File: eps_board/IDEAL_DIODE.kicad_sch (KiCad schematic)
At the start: 3 parts, among them U19 LTC4415

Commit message: final version with 48 pin connector: all boost/buck converters, 2 switched batt lines (though not connected to bus yet
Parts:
- renumbered R96 to R103, R97 to R104, U19 to U23
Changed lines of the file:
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@@
 		(on_board yes)
 		(dnp no)
-		(property "Reference" "U19"
+		(property "Reference" "U23"
 			(at 144.78 67.945 0)
 			(effects
@@
 			(project ""
 				(path "/05170af6-30ef-4c3a-b972-f098085da1bc/00000000-0000-0000-0000-00005f71f783"
-					(reference "U19")
+					(reference "U23")
 					(unit 1)
 				)
@@
 		(on_board yes)
 		(dnp no)
-		(property "Reference" "R96"
+		(property "Reference" "R103"
 			(at 115.57 85.09 90)
 			(effects
@@
 			(project ""
 				(path "/05170af6-30ef-4c3a-b972-f098085da1bc/00000000-0000-0000-0000-00005f71f783"
-					(reference "R96")
+					(reference "R103")
 					(unit 1)
 				)
@@
 		(on_board yes)
 		(dnp no)
-		(property "Reference" "R97"
+		(property "Reference" "R104"
 			(at 115.57 92.71 90)
 			(effects
@@
 			(project ""
 				(path "/05170af6-30ef-4c3a-b972-f098085da1bc/00000000-0000-0000-0000-00005f71f783"
-					(reference "R97")
+					(reference "R104")
 					(unit 1)
 				)

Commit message: changed from 48 pin connector to 40 pic PCA connector. remove uarts, ensure reset pins for all system components, attention pin to iniate IRQ on all components
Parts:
- renumbered R103 to R98, R104 to R99, U23 to U16
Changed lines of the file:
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@@
 		(on_board yes)
 		(dnp no)
-		(property "Reference" "U23"
+		(property "Reference" "U16"
 			(at 144.78 67.945 0)
 			(effects
@@
 			(project ""
 				(path "/05170af6-30ef-4c3a-b972-f098085da1bc/00000000-0000-0000-0000-00005f71f783"
-					(reference "U23")
+					(reference "U16")
 					(unit 1)
 				)
@@
 		(on_board yes)
 		(dnp no)
-		(property "Reference" "R103"
+		(property "Reference" "R98"
 			(at 115.57 85.09 90)
 			(effects
@@
 			(project ""
 				(path "/05170af6-30ef-4c3a-b972-f098085da1bc/00000000-0000-0000-0000-00005f71f783"
-					(reference "R103")
+					(reference "R98")
 					(unit 1)
 				)
@@
 		(on_board yes)
 		(dnp no)
-		(property "Reference" "R104"
+		(property "Reference" "R99"
 			(at 115.57 92.71 90)
 			(effects
@@
 			(project ""
 				(path "/05170af6-30ef-4c3a-b972-f098085da1bc/00000000-0000-0000-0000-00005f71f783"
-					(reference "R104")
+					(reference "R99")
 					(unit 1)
 				)

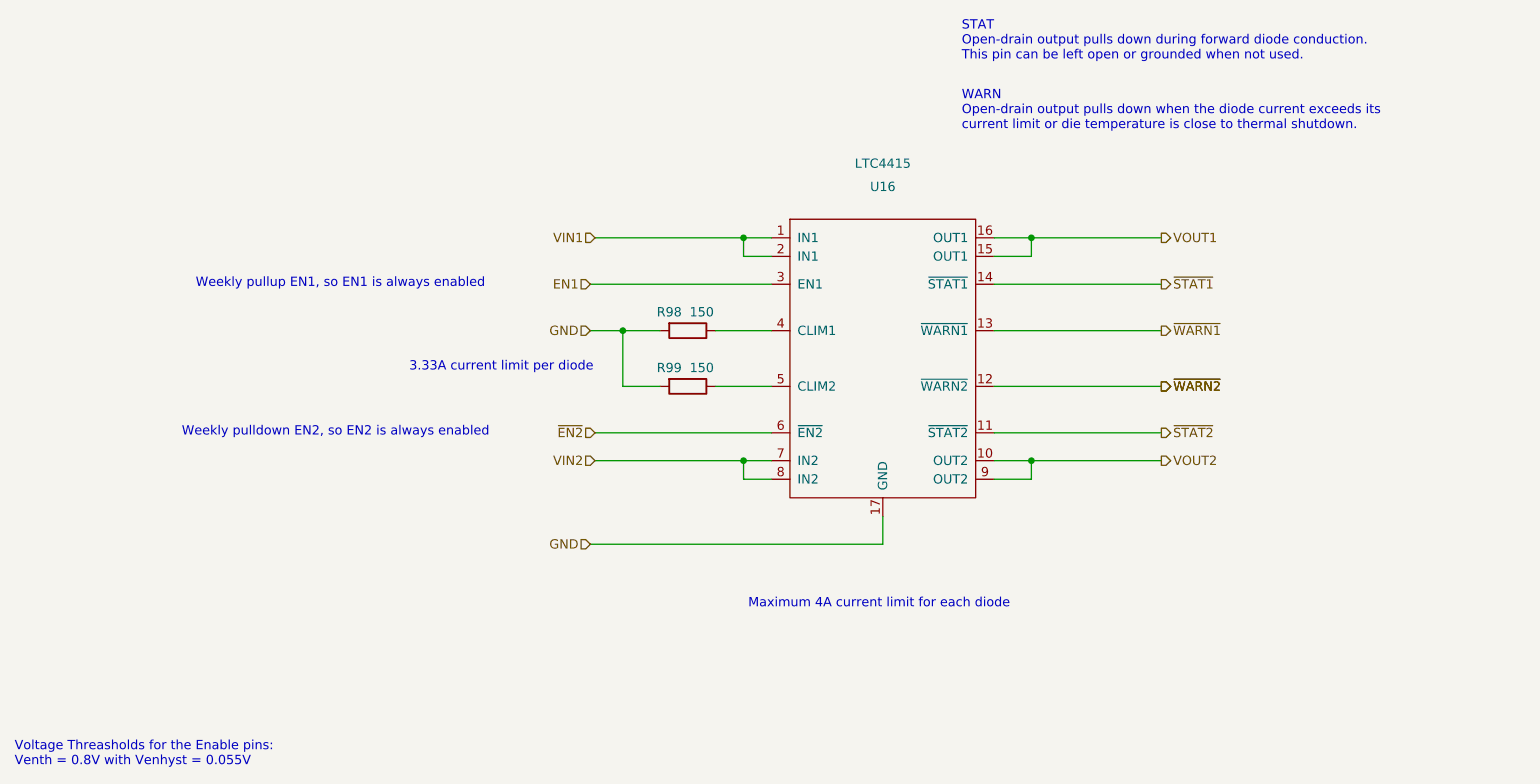
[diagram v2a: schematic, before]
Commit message: simply eps and automate startup conditions
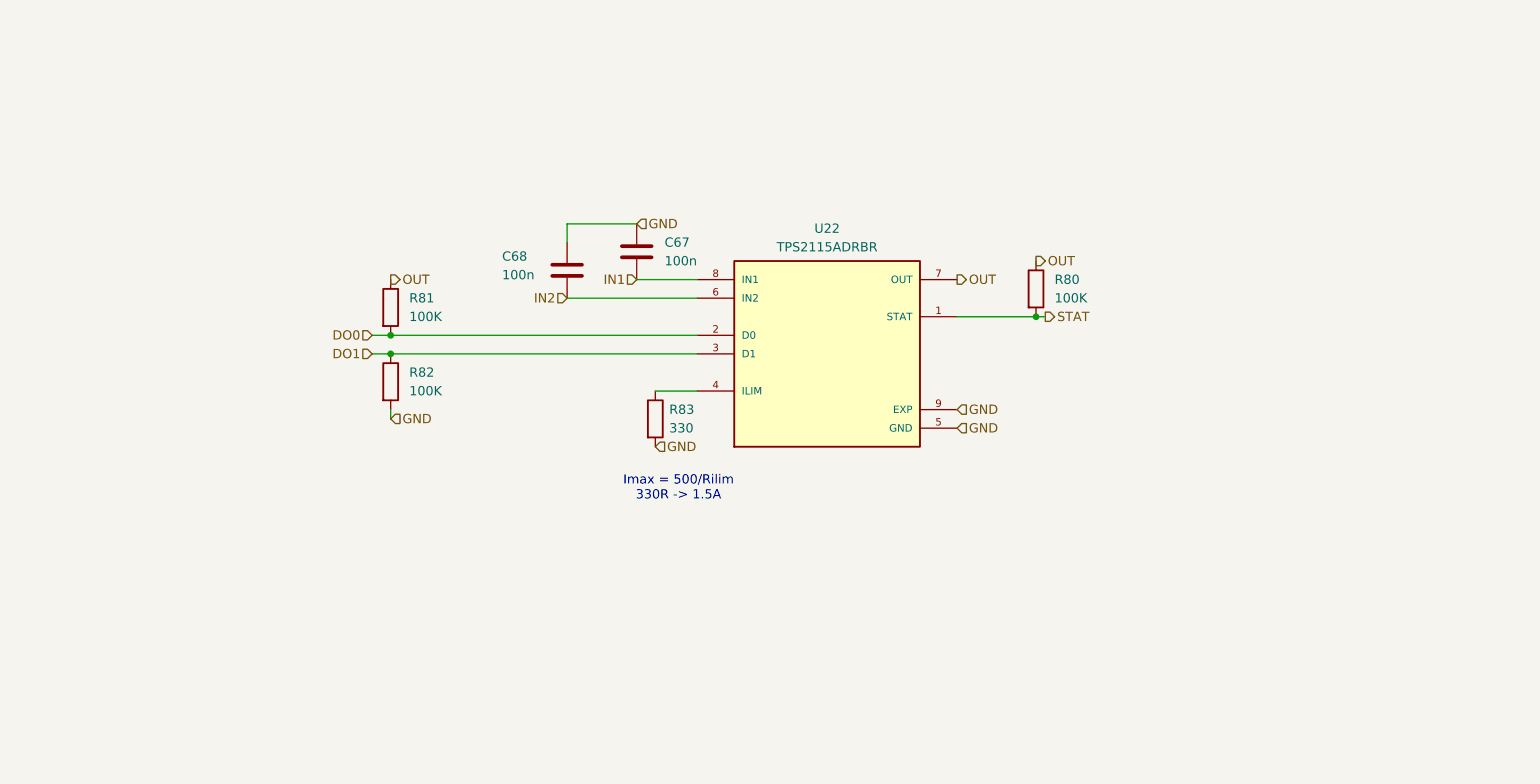
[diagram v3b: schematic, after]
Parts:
- removed R98, R99: 150, Resistor_SMD:R_0402_1005Metric_Pad0.72x0.64mm_HandSolder, symbol Device:R
- removed U16: LTC4415, Package_SO:MSOP-16-1EP_3x4.039mm_P0.5mm_EP1.651x2.845mm, symbol Project:LTC4415
- added C67, C68: 100n, Capacitor_SMD:C_0402_1005Metric_Pad0.74x0.62mm_HandSolder, symbol Device:C
- added R80, R81, R82: 100K, Resistor_SMD:R_0402_1005Metric_Pad0.72x0.64mm_HandSolder, symbol Device:R
- added R83: 330, Resistor_SMD:R_0402_1005Metric_Pad0.72x0.64mm_HandSolder, symbol Device:R
- added U22: TPS2115ADRBR, Common:SON65P300X300X100-9N, symbol Common:TPS2115ADRBR
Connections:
- net GND: now also C67.1, C68.1, R82.2, R83.2, U22.5 (GND), U22.9 (EXP)
- new net: R83.1, U22.4 (ILIM)
- new net DO0: R81.2, U22.2 (D0)
- new net DO1: R82.1, U22.3 (D1)
- new net IN1: C67.2, U22.8 (IN1)
- new net IN2: C68.2, U22.6 (IN2)
- new net OUT: R80.1, R81.1, U22.7 (OUT)
- new net STAT: R80.2, U22.1 (STAT)
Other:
- note added: "Imax = 500/Rilim 330R -> 1.5A"
- note removed: "3.33A current limit per diode"
- note removed: "Maximum 4A current limit for each diode"
- note removed: "STAT Open-drain output pulls down during forward diode conduction. This pin can be left open or grounded when not used."
- note removed: "Voltage Threasholds for the Enable pins: Venth = 0.8V with Venhyst = 0.055V"
- note removed: "WARN Open-drain output pulls down when the diode current exceeds its current limit or die temperature is close to thermal shutdown."
- note removed: "Weekly pulldown EN2, so EN2 is always enabled"
- note removed: "Weekly pullup EN1, so EN1 is always enabled"

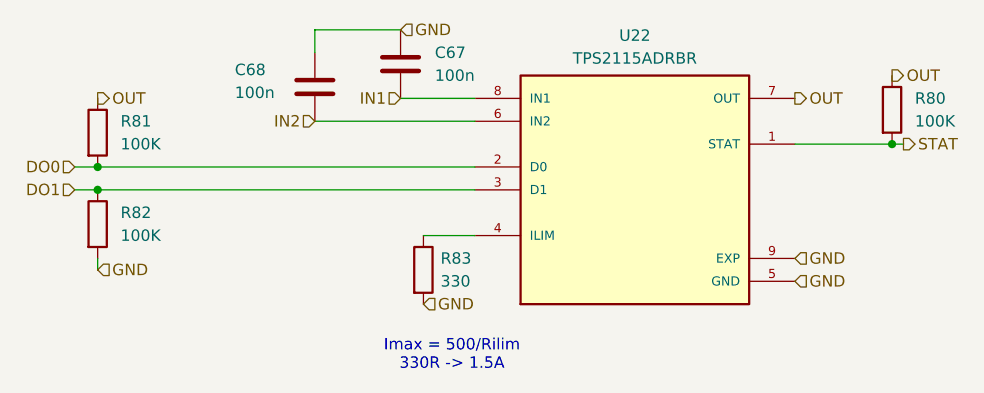
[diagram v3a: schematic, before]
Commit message: pcb and silk screen cleanup, interim
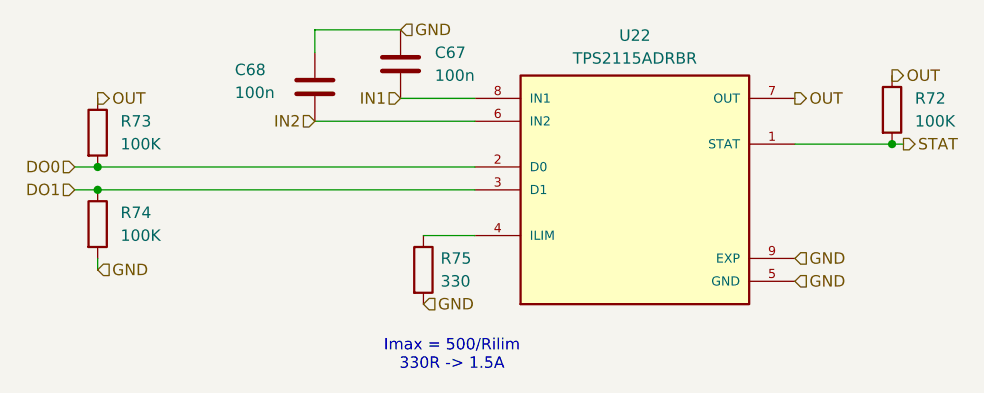
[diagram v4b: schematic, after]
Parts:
- renumbered R80 to R72, R81 to R73, R82 to R74, R83 to R75
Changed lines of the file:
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@@
 		(dnp no)
 		(fields_autoplaced yes)
-		(property "Reference" "R83"
+		(property "Reference" "R75"
 			(at 115.57 98.4249 0)
 			(effects
@@
 			(project "EPS"
 				(path "/05170af6-30ef-4c3a-b972-f098085da1bc/00000000-0000-0000-0000-00005f71f783"
-					(reference "R83")
+					(reference "R75")
 					(unit 1)
 				)
@@
 		(dnp no)
 		(fields_autoplaced yes)
-		(property "Reference" "R81"
+		(property "Reference" "R73"
 			(at 80.01 83.1849 0)
 			(effects
@@
 			(project "EPS"
 				(path "/05170af6-30ef-4c3a-b972-f098085da1bc/00000000-0000-0000-0000-00005f71f783"
-					(reference "R81")
+					(reference "R73")
 					(unit 1)
 				)
@@
 		(dnp no)
 		(fields_autoplaced yes)
-		(property "Reference" "R80"
+		(property "Reference" "R72"
 			(at 168.275 80.6449 0)
 			(effects
@@
 			(project "EPS"
 				(path "/05170af6-30ef-4c3a-b972-f098085da1bc/00000000-0000-0000-0000-00005f71f783"
-					(reference "R80")
+					(reference "R72")
 					(unit 1)
 				)
@@
 		(dnp no)
 		(fields_autoplaced yes)
-		(property "Reference" "R82"
+		(property "Reference" "R74"
 			(at 80.01 93.3449 0)
 			(effects
@@
 			(project ""
 				(path "/05170af6-30ef-4c3a-b972-f098085da1bc/00000000-0000-0000-0000-00005f71f783"
-					(reference "R82")
-					(unit 1)
-				)
+					(reference "R74")
+					(unit 1)
+				)

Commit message: light sensors with i2c multiplexers for AVI board. i2c amp/volt meter for attitude control coils
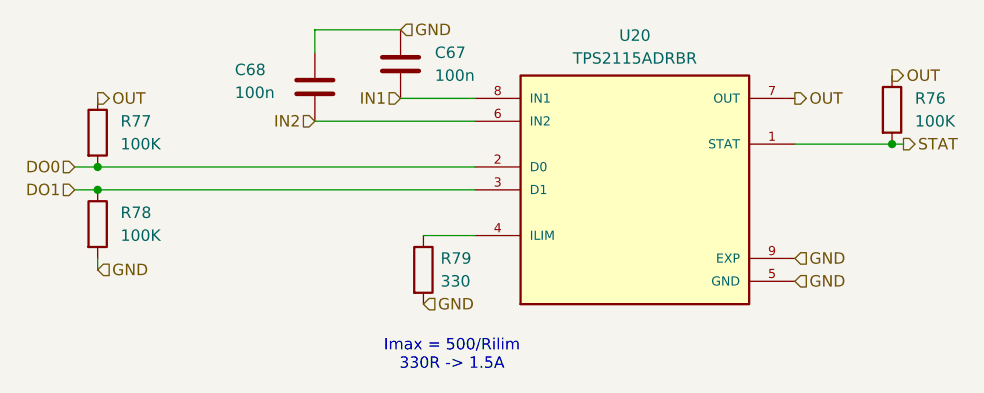
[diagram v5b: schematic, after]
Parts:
- renumbered R72 to R76, R73 to R77, R74 to R78, R75 to R79, U22 to U20
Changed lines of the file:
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@@
 		(dnp no)
 		(fields_autoplaced yes)
-		(property "Reference" "R75"
+		(property "Reference" "R79"
 			(at 115.57 98.4249 0)
 			(effects
@@
 			(project "EPS"
 				(path "/05170af6-30ef-4c3a-b972-f098085da1bc/00000000-0000-0000-0000-00005f71f783"
-					(reference "R75")
+					(reference "R79")
 					(unit 1)
 				)
@@
 		(dnp no)
 		(fields_autoplaced yes)
-		(property "Reference" "R73"
+		(property "Reference" "R77"
 			(at 80.01 83.1849 0)
 			(effects
@@
 			(project "EPS"
 				(path "/05170af6-30ef-4c3a-b972-f098085da1bc/00000000-0000-0000-0000-00005f71f783"
-					(reference "R73")
+					(reference "R77")
 					(unit 1)
 				)
@@
 		(dnp no)
 		(fields_autoplaced yes)
-		(property "Reference" "R72"
+		(property "Reference" "R76"
 			(at 168.275 80.6449 0)
 			(effects
@@
 			(project "EPS"
 				(path "/05170af6-30ef-4c3a-b972-f098085da1bc/00000000-0000-0000-0000-00005f71f783"
-					(reference "R72")
+					(reference "R76")
 					(unit 1)
 				)
@@
 		(dnp no)
 		(fields_autoplaced yes)
-		(property "Reference" "U22"
+		(property "Reference" "U20"
 			(at 137.16 73.66 0)
 			(effects
@@
 			(project ""
 				(path "/05170af6-30ef-4c3a-b972-f098085da1bc/00000000-0000-0000-0000-00005f71f783"
-					(reference "U22")
+					(reference "U20")
 					(unit 1)
 				)
@@
 		(dnp no)
 		(fields_autoplaced yes)
-		(property "Reference" "R74"
+		(property "Reference" "R78"
 			(at 80.01 93.3449 0)
 			(effects
@@
 			(project ""
 				(path "/05170af6-30ef-4c3a-b972-f098085da1bc/00000000-0000-0000-0000-00005f71f783"
-					(reference "R74")
-					(unit 1)
-				)
+					(reference "R78")
+					(unit 1)
+				)

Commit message: interim checkin for EPS BOM
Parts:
- C67, C68: value 100n -> 100nF; Manufacturer (none) -> Murata; Part Number (none) -> GRM155R61E104KA87D; Tolerance (none) -> 10; Voltage (none) -> 25
- R76, R77, R78: Manufacturer (none) -> YAGEO; Part Number (none) -> RC0402FR-07100KL; Tolerance (none) -> 1
- R79: Manufacturer (none) -> YAGEO; Part Number (none) -> RC0402FR-07330RL; Tolerance (none) -> 1
- U20: AVAILABILITY Warning -> (none); MF Texas Instruments -> (none); MOUSER-PURCHASE-URL https://snapeda.com/shop?store=Mouser&id=391793 -> (none); MP TPS2115ADRBR -> (none); PACKAGE VSON-8 Texas Instruments -> (none); PRICE None -> (none); TEXAS_INSTRUMENTS-PURCHASE-URL https://snapeda.com/shop?store=Texas+Instruments&id=391793 -> (none)
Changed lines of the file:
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@@
 			)
 		)
-		(property "Datasheet" "~"
+		(property "Datasheet" "https://www.yageo.com/upload/media/product/products/datasheet/rchip/PYu-RC_Group_51_RoHS_L_12.pdf"
 			(at 113.665 99.695 0)
 			(effects
@@
 		)
 		(property "Description" "Resistor"
+			(at 113.665 99.695 0)
+			(effects
+				(font
+					(size 1.27 1.27)
+				)
+				(hide yes)
+			)
+		)
+		(property "Manufacturer" "YAGEO"
+			(at 113.665 99.695 0)
+			(effects
+				(font
+					(size 1.27 1.27)
+				)
+				(hide yes)
+			)
+		)
+		(property "Part Number" "RC0402FR-07330RL"
+			(at 113.665 99.695 0)
+			(effects
+				(font
+					(size 1.27 1.27)
+				)
+				(hide yes)
+			)
+		)
+		(property "Tolerance" "1"
 			(at 113.665 99.695 0)
 			(effects
@@
 			)
 		)
-		(property "Datasheet" "~"
+		(property "Datasheet" "https://www.yageo.com/upload/media/product/products/datasheet/rchip/PYu-RC_Group_51_RoHS_L_12.pdf"
 			(at 77.47 84.455 0)
 			(effects
@@
 		)
 		(property "Description" "Resistor"
+			(at 77.47 84.455 0)
+			(effects
+				(font
+					(size 1.27 1.27)
+				)
+				(hide yes)
+			)
+		)
+		(property "Manufacturer" "YAGEO"
+			(at 77.47 84.455 0)
+			(effects
+				(font
+					(size 1.27 1.27)
+				)
+				(hide yes)
+			)
+		)
+		(property "Part Number" "RC0402FR-07100KL"
+			(at 77.47 84.455 0)
+			(effects
+				(font
+					(size 1.27 1.27)
+				)
+				(hide yes)
+			)
+		)
+		(property "Tolerance" "1"
 			(at 77.47 84.455 0)
 			(effects
@@
 			)
 		)
-		(property "Datasheet" "~"
+		(property "Datasheet" "https://www.yageo.com/upload/media/product/products/datasheet/rchip/PYu-RC_Group_51_RoHS_L_12.pdf"
 			(at 165.735 81.915 0)
 			(effects
@@
 		)
 		(property "Description" "Resistor"
+			(at 165.735 81.915 0)
+			(effects
+				(font
+					(size 1.27 1.27)
+				)
+				(hide yes)
+			)
+		)
+		(property "Manufacturer" "YAGEO"
+			(at 165.735 81.915 0)
+			(effects
+				(font
+					(size 1.27 1.27)
+				)
+				(hide yes)
+			)
+		)
+		(property "Part Number" "RC0402FR-07100KL"
+			(at 165.735 81.915 0)
+			(effects
+				(font
+					(size 1.27 1.27)
+				)
+				(hide yes)
+			)
+		)
+		(property "Tolerance" "1"
 			(at 165.735 81.915 0)
 			(effects
@@
 			)
 		)
-		(property "MF" "Texas Instruments"
-			(at 137.16 90.805 0)
-			(effects
-				(font
-					(size 1.27 1.27)
-				)
-				(justify bottom)
-				(hide yes)
-			)
-		)
-		(property "MOUSER-PURCHASE-URL" "https://snapeda.com/shop?store=Mouser&id=391793"
-			(at 137.16 90.805 0)
-			(effects
-				(font
-					(size 1.27 1.27)
-				)
-				(justify bottom)
-				(hide yes)
-			)
-		)
-		(property "PACKAGE" "VSON-8 Texas Instruments"
-			(at 137.16 90.805 0)
-			(effects
-				(font
-					(size 1.27 1.27)
-				)
-				(justify bottom)
-				(hide yes)
-			)
-		)
-		(property "PRICE" "None"
-			(at 137.16 90.805 0)
-			(effects
-				(font
-					(size 1.27 1.27)
-				)
-				(justify bottom)
-				(hide yes)
-			)
-		)
-		(property "MP" "TPS2115ADRBR"
-			(at 137.16 90.805 0)
-			(effects
-				(font
-					(size 1.27 1.27)
-				)
-				(justify bottom)
-				(hide yes)
-			)
-		)
-		(property "TEXAS_INSTRUMENTS-PURCHASE-URL" "https://snapeda.com/shop?store=Texas+Instruments&id=391793"
-			(at 137.16 90.805 0)
-			(effects
-				(font
-					(size 1.27 1.27)
-				)
-				(justify bottom)
-				(hide yes)
-			)
-		)
-		(property "AVAILABILITY" "Warning"
-			(at 137.16 90.805 0)
-			(effects
-				(font
-					(size 1.27 1.27)
-				)
-				(justify bottom)
-				(hide yes)
-			)
-		)
 		(pin "9"
 		)
@@
 			)
 		)
-		(property "Value" "100n"
+		(property "Value" "100nF"
 			(at 114.935 78.1049 0)
 			(effects
@@
 			)
 		)
-		(property "Datasheet" "~"
+		(property "Datasheet" "https://search.murata.co.jp/Ceramy/image/img/A01X/G101/ENG/GRM155R61E104KA87-01.pdf"
 			(at 111.125 76.835 0)
 			(effects
@@
 		)
 		(property "Description" "Unpolarized capacitor"
+			(at 111.125 76.835 0)
+			(effects
+				(font
+					(size 1.27 1.27)
+				)
+				(hide yes)
+			)
+		)
+		(property "Manufacturer" "Murata"
+			(at 111.125 76.835 0)
+			(effects
+				(font
+					(size 1.27 1.27)
+				)
+				(hide yes)
+			)
+		)
+		(property "Part Number" "GRM155R61E104KA87D"
+			(at 111.125 76.835 0)
+			(effects
+				(font
+					(size 1.27 1.27)
+				)
+				(hide yes)
+			)
+		)
+		(property "Voltage" "25"
+			(at 111.125 76.835 0)
+			(effects
+				(font
+					(size 1.27 1.27)
+				)
+				(hide yes)
+			)
+		)
+		(property "Tolerance" "10"
 			(at 111.125 76.835 0)
 			(effects
@@
 			)
 		)
-		(property "Datasheet" "~"
+		(property "Datasheet" "https://www.yageo.com/upload/media/product/products/datasheet/rchip/PYu-RC_Group_51_RoHS_L_12.pdf"
 			(at 77.47 94.615 0)
 			(effects
@@
 		)
 		(property "Description" "Resistor"
+			(at 77.47 94.615 0)
+			(effects
+				(font
+					(size 1.27 1.27)
+				)
+				(hide yes)
+			)
+		)
+		(property "Manufacturer" "YAGEO"
+			(at 77.47 94.615 0)
+			(effects
+				(font
+					(size 1.27 1.27)
+				)
+				(hide yes)
+			)
+		)
+		(property "Part Number" "RC0402FR-07100KL"
+			(at 77.47 94.615 0)
+			(effects
+				(font
+					(size 1.27 1.27)
+				)
+				(hide yes)
+			)
+		)
+		(property "Tolerance" "1"
 			(at 77.47 94.615 0)
 			(effects
@@
 			)
 		)
-		(property "Value" "100n"
+		(property "Value" "100nF"
 			(at 92.71 80.01 0)
 			(effects
@@
 			)
 		)
-		(property "Datasheet" "~"
+		(property "Datasheet" "https://search.murata.co.jp/Ceramy/image/img/A01X/G101/ENG/GRM155R61E104KA87-01.pdf"
 			(at 101.6 79.375 0)
 			(effects
@@
 			(at 101.6 79.375 0)
 			(effects
+				(font
+					(size 1.27 1.27)
+				)
+				(hide yes)
+			)
+		)
+		(property "Manufacturer" "Murata"
+			(at 101.6 79.375 0)
+			(effects
+				(font
+					(size 1.27 1.27)
+				)
+				(hide yes)
+			)
+		)
+		(property "Part Number" "GRM155R61E104KA87D"
+			(at 101.6 79.375 0)
+			(effects
+				(font
+					(size 1.27 1.27)
+				)
+				(hide yes)
+			)
+		)
+		(property "Voltage" "25"
+			(at 101.6 79.375 0)
+			(effects
+				(font
+					(size 1.27 1.27)
+				)
+				(hide yes)
+			)
+		)
+		(property "Tolerance" "10"
+			(at 101.6 79.375 0)
+			(effects

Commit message: complete BOM assignment for EPS, next step circular check and deep dives
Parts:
- U20: Manufacturer (none) -> TI; Part Number (none) -> TPS2115ADRBR
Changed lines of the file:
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@@
+			)
+		)
+		(property "Manufacturer" "TI"
+			(at 137.16 90.805 0)
+			(effects
+				(font
+					(size 1.27 1.27)
+				)
+				(hide yes)
+			)
+		)
+		(property "Part Number" "TPS2115ADRBR "
+			(at 137.16 90.805 0)
+			(effects
+				(font
+					(size 1.27 1.27)
+				)
+				(hide yes)
 			)
 		)
